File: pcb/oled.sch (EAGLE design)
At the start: 18 parts, among them U1 UG-2828GDEDF11, U3 FAN5331SX

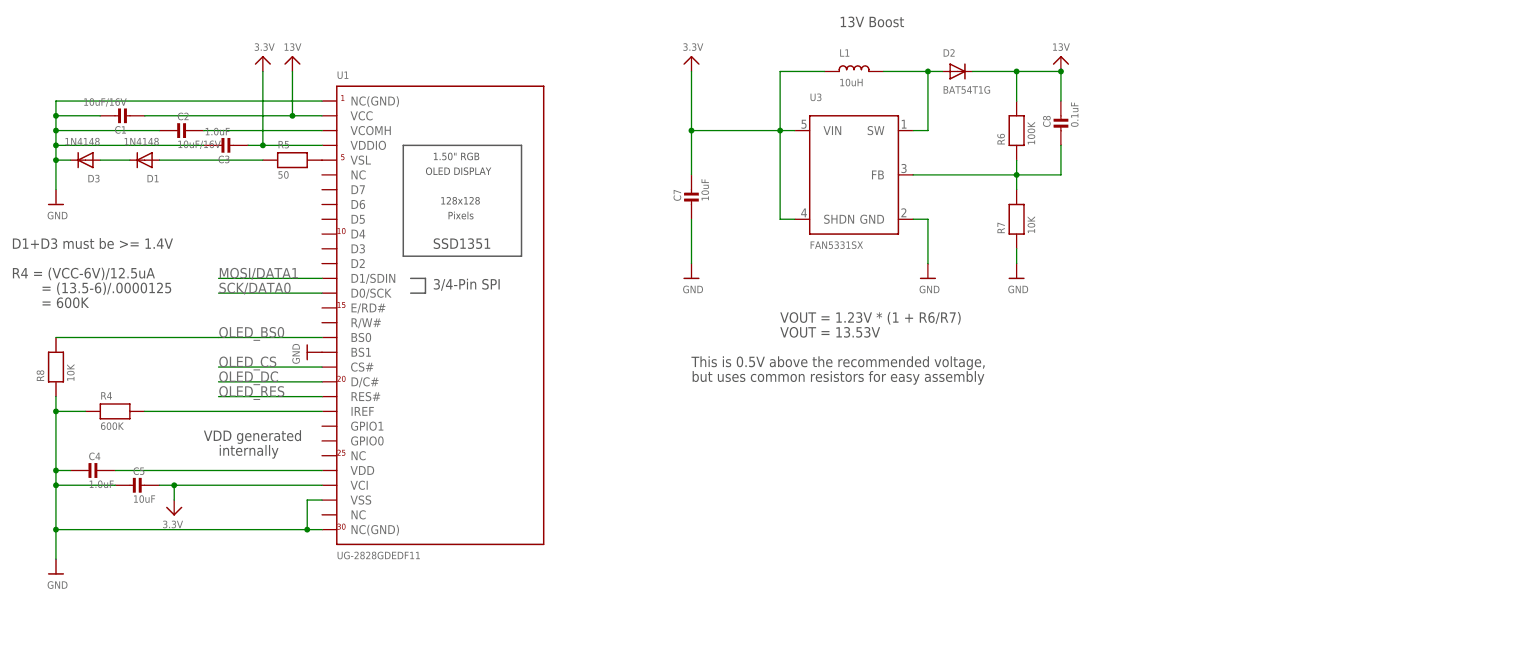
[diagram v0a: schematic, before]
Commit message: oled board ready to be fab'd
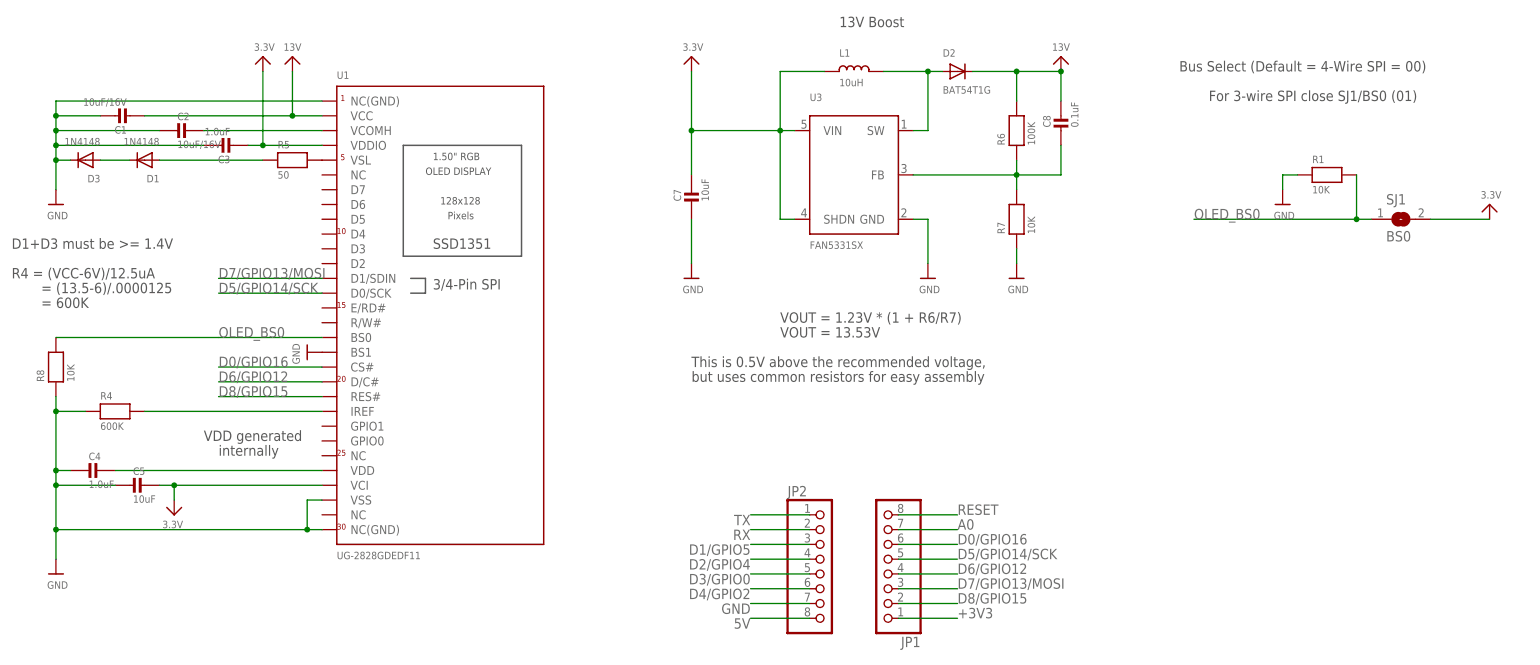
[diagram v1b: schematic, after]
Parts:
- added JP1, JP2: (no value), adafruit:PINHD-1X8CLEANBIG
- added R1: 10K, microbuilder:RESISTOR_0805MP
- added SJ1: BS0, microbuilder:SOLDERJUMPERREFLOW_NOPASTE
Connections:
- removed net 3.3V: C3.P$2, C5.P$1, C7.P$1, L1.1, U1.VCI, U1.VDDIO, U3.SHDN, U3.VIN
- removed net MOSI/DATA1: U1.D1/SDIN
- removed net OLED_CS: U1.CS#
- removed net OLED_DC: U1.D/C#
- removed net OLED_RES: U1.RES#
- removed net SCK/DATA0: U1.D0/SCK
- new net +3V3: C3.P$2, C5.P$1, C7.P$1, JP1.1, L1.1, SJ1.2, U1.VCI, U1.VDDIO, U3.SHDN, U3.VIN
- new net 5V: JP2.8
- new net A0: JP1.7
- new net D0/GPIO16: JP1.6, U1.CS#
- new net D1/GPIO5: JP2.3
- new net D2/GPIO4: JP2.4
- new net D3/GPIO0: JP2.5
- new net D4/GPIO2: JP2.6
- new net D5/GPIO14/SCK: JP1.5, U1.D0/SCK
- new net D6/GPIO12: JP1.4, U1.D/C#
- new net D7/GPIO13/MOSI: JP1.3, U1.D1/SDIN
- new net D8/GPIO15: JP1.2, U1.RES#
- new net RESET: JP1.8
- new net RX: JP2.2
- new net TX: JP2.1
- net GND: now also JP2.7, R1.1
- net OLED_BS0: now also R1.2, SJ1.1
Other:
- note added: "Bus Select (Default = 4-Wire SPI = 00)"
- note added: "For 3-wire SPI close SJ1/BS0 (01)"

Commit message: USB board schematic V2 done
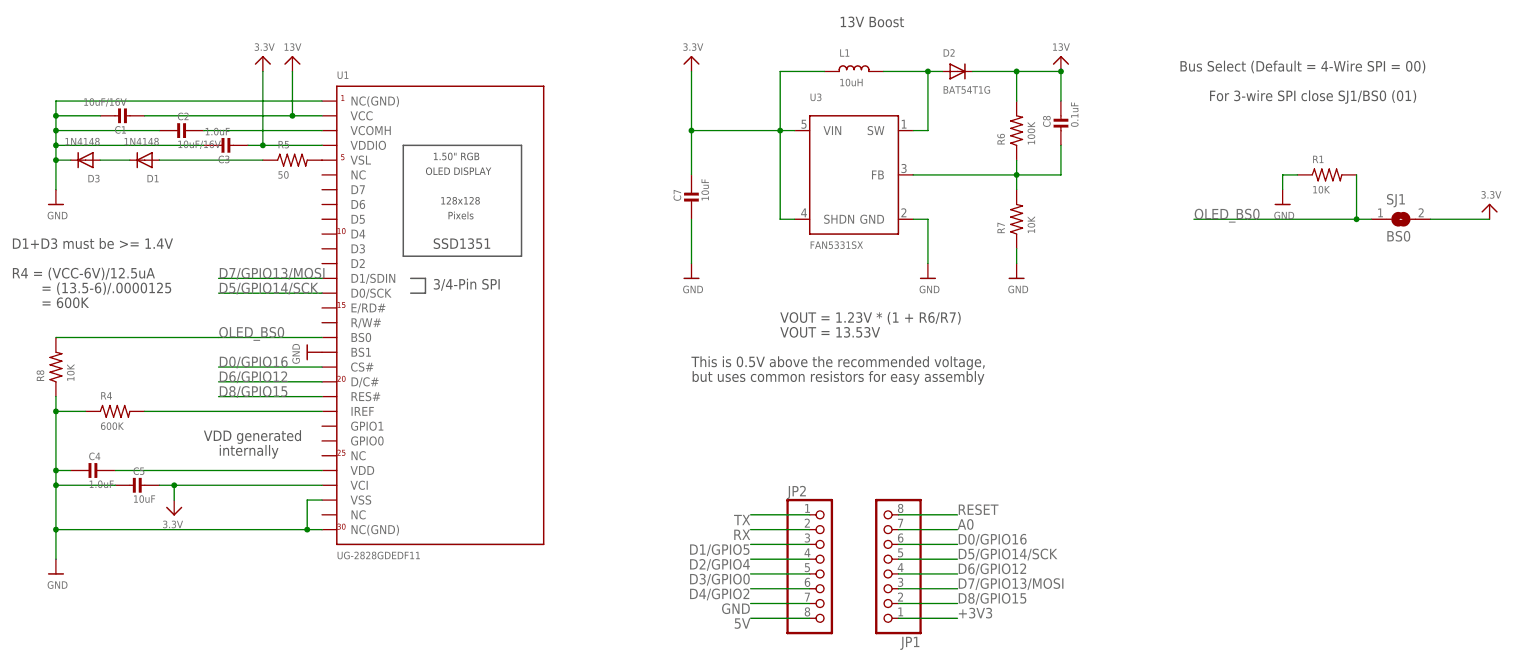
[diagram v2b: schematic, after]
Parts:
- R1: device microbuilder:RESISTOR_0805MP -> adafruit:R-US_R0805
- R4, R5, R6, R7, R8: device microbuilder:RESISTOR0805 -> adafruit:R-US_R0805
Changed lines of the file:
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@@
 <parts>
 <part name="U$4" library="microbuilder" deviceset="GND" device=""/>
-<part name="R4" library="microbuilder" deviceset="RESISTOR" device="0805" value="600K"/>
+<part name="R4" library="adafruit" library_urn="urn:adsk.eagle:library:420" deviceset="R-US_" device="R0805" package3d_urn="urn:adsk.eagle:package:6240566/1" value="600K"/>
 <part name="C1" library="microbuilder" deviceset="CAP_CERAMIC" device="0805" value="10uF/16V"/>
 <part name="C3" library="microbuilder" deviceset="CAP_CERAMIC" device="0805" value="1.0uF"/>
-<part name="R5" library="microbuilder" deviceset="RESISTOR" device="0805" value="50"/>
+<part name="R5" library="adafruit" library_urn="urn:adsk.eagle:library:420" deviceset="R-US_" device="R0805" package3d_urn="urn:adsk.eagle:package:6240566/1" value="50"/>
 <part name="D1" library="microbuilder" deviceset="DIODE" device="SOD-323" value="1N4148"/>
 <part name="C4" library="microbuilder" deviceset="CAP_CERAMIC" device="0805" value="1.0uF"/>
@@
 <part name="L1" library="microbuilder" deviceset="INDUCTOR" device="" value="10uH"/>
 <part name="D2" library="microbuilder" deviceset="DIODE" device="SOD-123" value="BAT54T1G"/>
-<part name="R6" library="microbuilder" deviceset="RESISTOR" device="0805" value="100K"/>
-<part name="R7" library="microbuilder" deviceset="RESISTOR" device="0805" value="10K"/>
+<part name="R6" library="adafruit" library_urn="urn:adsk.eagle:library:420" deviceset="R-US_" device="R0805" package3d_urn="urn:adsk.eagle:package:6240566/1" value="100K"/>
+<part name="R7" library="adafruit" library_urn="urn:adsk.eagle:library:420" deviceset="R-US_" device="R0805" package3d_urn="urn:adsk.eagle:package:6240566/1" value="10K"/>
 <part name="U$11" library="microbuilder" deviceset="GND" device=""/>
 <part name="U$12" library="microbuilder" deviceset="GND" device=""/>
@@
 <part name="D3" library="microbuilder" deviceset="DIODE" device="SOD-323" value="1N4148"/>
 <part name="U$3" library="microbuilder" deviceset="GND" device=""/>
-<part name="R8" library="microbuilder" deviceset="RESISTOR" device="0805" value="10K"/>
+<part name="R8" library="adafruit" library_urn="urn:adsk.eagle:library:420" deviceset="R-US_" device="R0805" package3d_urn="urn:adsk.eagle:package:6240566/1" value="10K"/>
 <part name="JP1" library="adafruit" library_urn="urn:adsk.eagle:library:420" deviceset="PINHD-1X8" device="CLEANBIG" package3d_urn="urn:adsk.eagle:package:6240708/1"/>
 <part name="JP2" library="adafruit" library_urn="urn:adsk.eagle:library:420" deviceset="PINHD-1X8" device="CLEANBIG" package3d_urn="urn:adsk.eagle:package:6240708/1"/>
 <part name="SJ1" library="microbuilder" deviceset="SOLDERJUMPER" device="REFLOW_NOPASTE" value="BS0"/>
-<part name="R1" library="microbuilder" deviceset="RESISTOR" device="_0805MP" value="10K"/>
+<part name="R1" library="adafruit" library_urn="urn:adsk.eagle:library:420" deviceset="R-US_" device="R0805" package3d_urn="urn:adsk.eagle:package:6240566/1" value="10K"/>
 <part name="U$2" library="microbuilder" deviceset="3.3V" device=""/>
 <part name="U$6" library="microbuilder" deviceset="GND" device=""/>

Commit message: Rework Oled board to use VIN
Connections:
- removed net 5V: JP2.8
- new net VIN: C7.P$1, JP2.8, L1.1, U3.SHDN, U3.VIN
- net +3V3: no longer C7.P$1, L1.1, U3.SHDN, U3.VIN

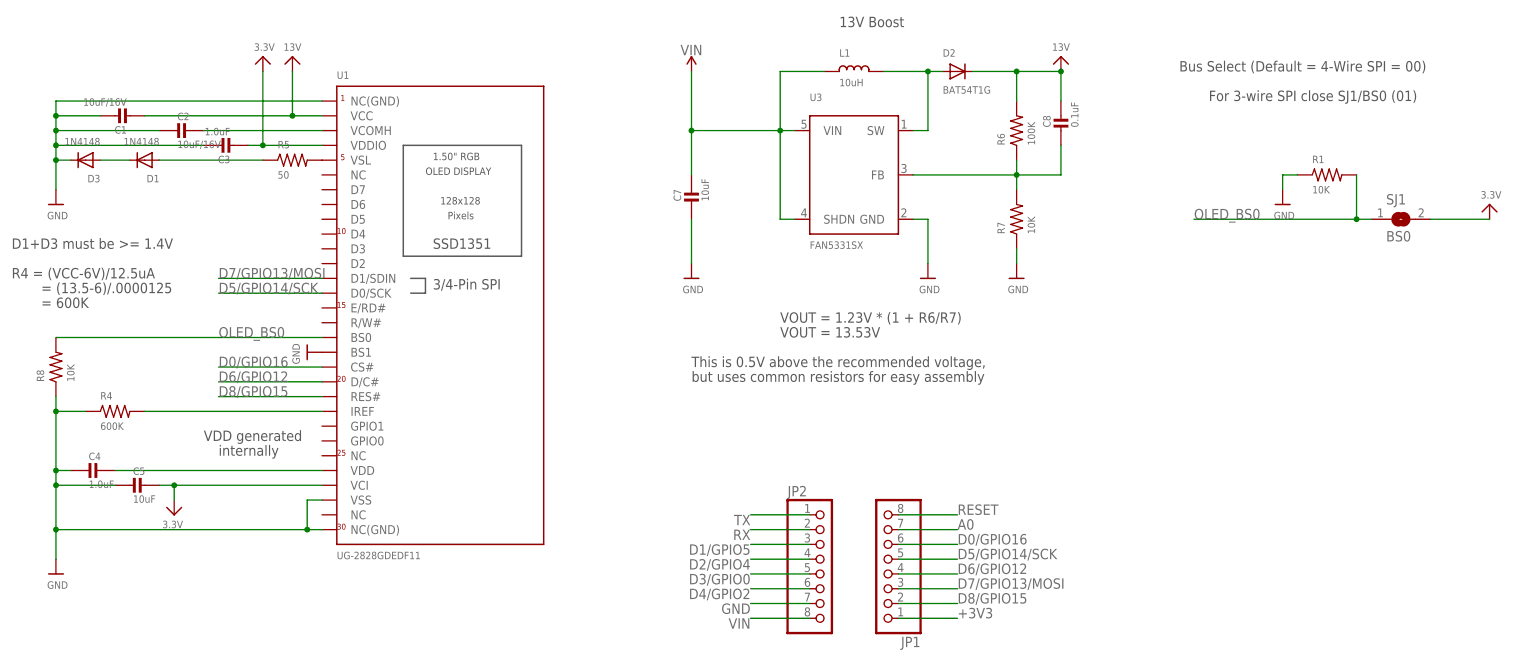
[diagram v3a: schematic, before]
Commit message: V2 oled board ordered
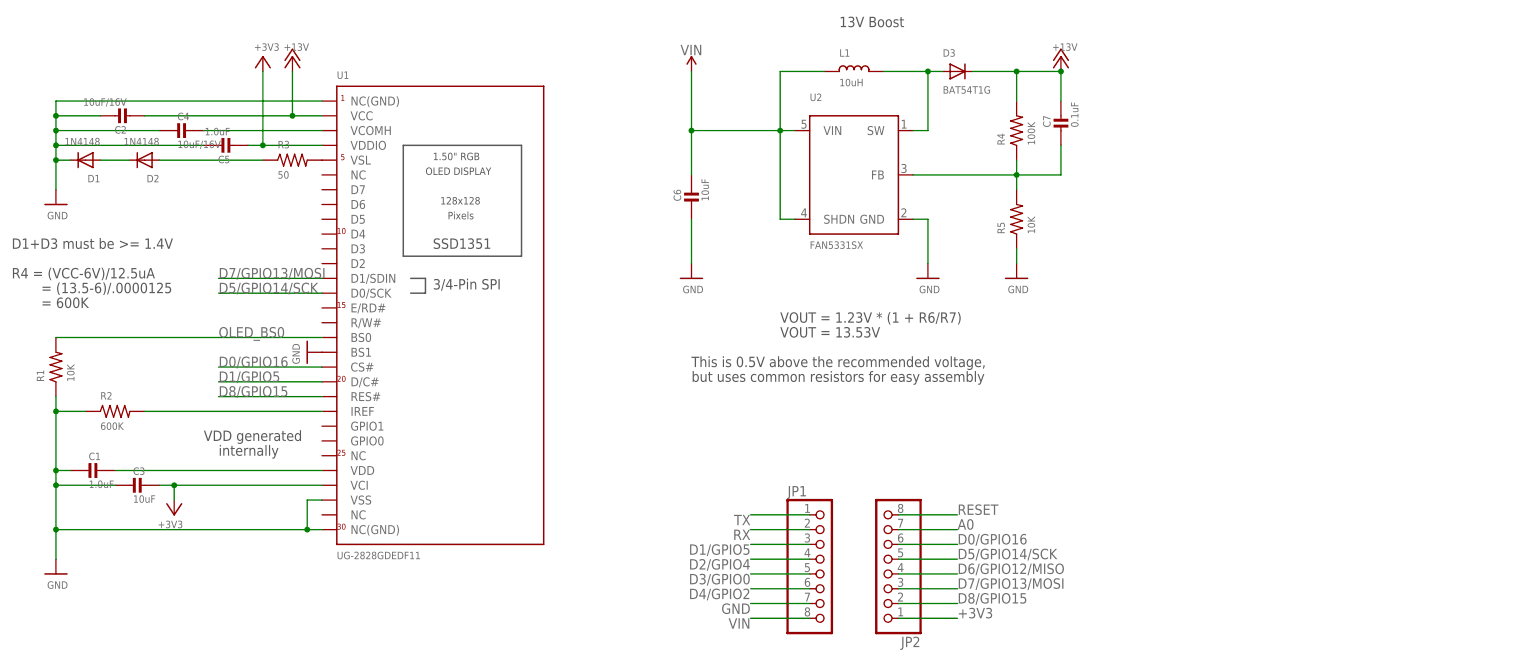
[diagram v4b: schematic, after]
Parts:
- removed C8: 0.1uF, microbuilder:CAP_CERAMIC0805
- removed R6: 100K, adafruit:R-US_R0805
- removed R7, R8: 10K, adafruit:R-US_R0805
- removed SJ1: BS0, microbuilder:SOLDERJUMPERREFLOW_NOPASTE
- added C6: 10uF, microbuilder:CAP_CERAMIC0805
- added R2: 600K, adafruit:R-US_R0805
- added R3: 50, adafruit:R-US_R0805
- C1: value 10uF/16V -> 1.0uF
- C3: value 1.0uF -> 10uF
- C4: value 1.0uF -> 10uF/16V
- C5: value 10uF -> 1.0uF
- C7: value 10uF -> 0.1uF
- D2: value BAT54T1G -> 1N4148; device microbuilder:DIODESOD-123 -> microbuilder:DIODESOD-323
- D3: value 1N4148 -> BAT54T1G; device microbuilder:DIODESOD-323 -> microbuilder:DIODESOD-123
- R4: value 600K -> 100K
- R5: value 50 -> 10K
- renumbered U3 to U2
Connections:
- removed net D6/GPIO12: JP1.4, U1.D/C#
- new net D6/GPIO12/MISO: JP2.4
- net +3V3: now also C3.P$1, C5.P$2, JP2.1; no longer C3.P$2, C5.P$1, JP1.1, SJ1.2
- net 13V: now also C2.P$2, C7.P$1, D3.C, R4.2; no longer C1.P$2, C8.P$1, D2.C, R6.2
- net A0: now also JP2.7; no longer JP1.7
- net D0/GPIO16: now also JP2.6; no longer JP1.6
- net D1/GPIO5: now also JP1.3, U1.D/C#; no longer JP2.3
- net D2/GPIO4: now also JP1.4; no longer JP2.4
- net D3/GPIO0: now also JP1.5; no longer JP2.5
- net D4/GPIO2: now also JP1.6; no longer JP2.6
- net D5/GPIO14/SCK: now also JP2.5; no longer JP1.5
- net D7/GPIO13/MOSI: now also JP2.3; no longer JP1.3
- net D8/GPIO15: now also JP2.2; no longer JP1.2
- net GND: now also C1.P$2, C2.P$1, C3.P$2, C5.P$1, C6.P$2, D1.C, JP1.7, R2.1, R5.1; no longer C1.P$1, C2.P$2, C3.P$1, C5.P$2, C7.P$2, D3.C, JP2.7, R4.1, R7.1, R8.1
- net IREF: now also R2.2; no longer R4.2
- net N$11: now also D1.A, D2.C; no longer D1.C, D3.A
- net N$3: now also C1.P$1; no longer C4.P$1
- net N$5: now also D3.A; no longer D2.A
- net N$6: now also R3.2; no longer R5.2
- net N$7: now also D2.A, R3.1; no longer D1.A, R5.1
- net N$8: now also C7.P$2, R4.1, R5.2; no longer C8.P$2, R6.1, R7.2
- net OLED_BS0: no longer R8.2, SJ1.1
- net RESET: now also JP2.8; no longer JP1.8
- net RX: now also JP1.2; no longer JP2.2
- net TX: now also JP1.1; no longer JP2.1
- net VCOMH: now also C4.P$1; no longer C2.P$1
- net VIN: now also C6.P$1, JP1.8; no longer C7.P$1, JP2.8
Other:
- note removed: "Bus Select (Default = 4-Wire SPI = 00)"
- note removed: "For 3-wire SPI close SJ1/BS0 (01)"
- moved on the sheet: C1, C2, C3, C4, C5, C7, D1, D2, D3, JP1, JP2, R1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

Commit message: Add a bunch of manufacturer part numbers to OLED board
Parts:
- C1, C5: MPN (none) -> C0805C105K4RAC7210
- C2, C3, C4, C6: MPN (none) -> EMK212ABJ106KG-T
- C7: MPN (none) -> 08051C104J4T4A
- D1, D2: MPN (none) -> 1N4148WS-E3-08
- D3: MPN (none) -> BAT54T1G
- JP1, JP2: POPULATE (none) -> 0
- L1: MPN (none) -> L0805R100MPWRT
- R1, R5: MPN (none) -> CRCW080510K0FKEAC
- R2: MPN (none) -> ERJ-6ENF5903V
- R3: MPN (none) -> CRCW080550R0FKTA
- R4: MPN (none) -> CR0805AFX-1003EAS
- U1: MPN (none) -> XF2M-3015-1A
- U2: MPN (none) -> FAN5331SX

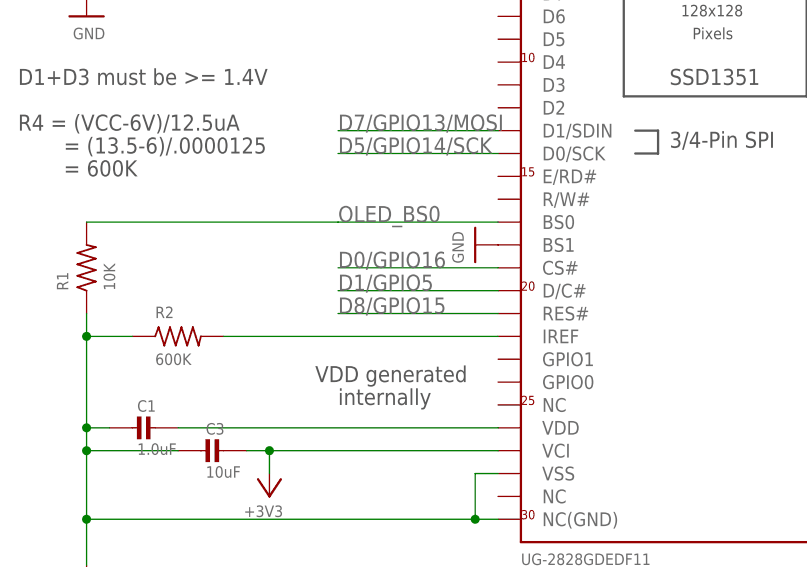
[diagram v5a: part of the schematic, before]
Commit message: Use GPIO2 instead of GPIO5(SCL) for OLED DC pin
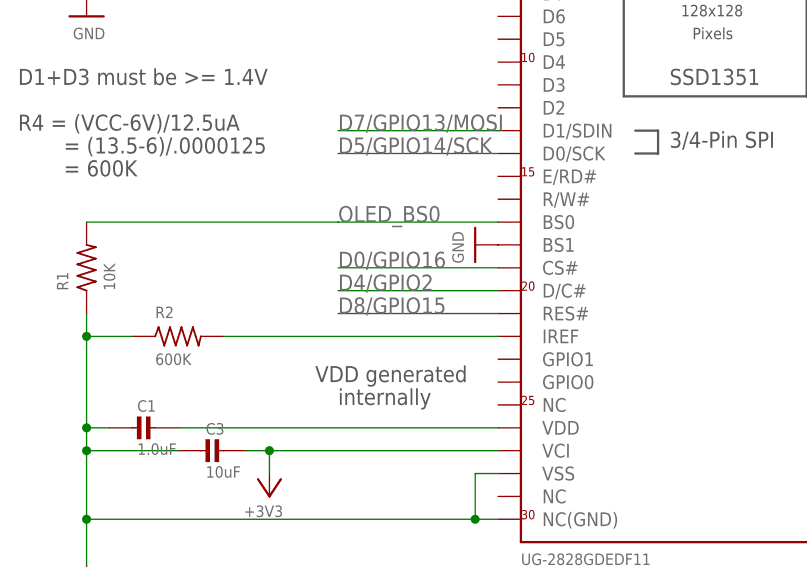
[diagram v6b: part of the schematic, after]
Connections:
- net D1/GPIO5: no longer U1.D/C#
- net D4/GPIO2: now also U1.D/C#
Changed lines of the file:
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@@
 <label x="203.2" y="96.52" size="1.778" layer="95" rot="R180"/>
-</segment>
-<segment>
-<wire x1="129.54" y1="124.46" x2="111.76" y2="124.46" width="0.1524" layer="91"/>
-<label x="111.76" y="124.46" size="1.778" layer="95"/>
-<pinref part="U1" gate="G$1" pin="D/C#"/>
 </segment>
 </net>
@@
 <label x="203.2" y="88.9" size="1.778" layer="95" rot="R180"/>
 </segment>
+<segment>
+<wire x1="129.54" y1="124.46" x2="111.76" y2="124.46" width="0.1524" layer="91"/>
+<label x="111.76" y="124.46" size="1.778" layer="95"/>
+<pinref part="U1" gate="G$1" pin="D/C#"/>
+</segment>
 </net>

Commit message: Oled board v3 ordered
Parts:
- JP1, JP2: MPN (none) -> 10129378-908001BLF
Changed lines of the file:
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@@
 </part>
 <part name="JP2" library="adafruit" library_urn="urn:adsk.eagle:library:420" deviceset="PINHD-1X8" device="CLEANBIG" package3d_urn="urn:adsk.eagle:package:6240708/1">
+<attribute name="MPN" value="10129378-908001BLF"/>
 <attribute name="POPULATE" value="0"/>
 </part>
 <part name="JP1" library="adafruit" library_urn="urn:adsk.eagle:library:420" deviceset="PINHD-1X8" device="CLEANBIG" package3d_urn="urn:adsk.eagle:package:6240708/1">
+<attribute name="MPN" value="10129378-908001BLF"/>
 <attribute name="POPULATE" value="0"/>
 </part>
@@
 <attribute name="VALUE" x="232.41" y="106.68" size="1.778" layer="96" rot="R180"/>
 <attribute name="POPULATE" x="226.06" y="91.44" size="1.778" layer="96" rot="R180" display="off"/>
+<attribute name="MPN" x="226.06" y="91.44" size="1.778" layer="96" rot="R180" display="off"/>
 </instance>
 <instance part="JP1" gate="G$1" x="215.9" y="93.98" smashed="yes">
@@
 <attribute name="VALUE" x="209.55" y="78.74" size="1.778" layer="96"/>
 <attribute name="POPULATE" x="215.9" y="93.98" size="1.778" layer="96" display="off"/>
+<attribute name="MPN" x="215.9" y="93.98" size="1.778" layer="96" display="off"/>
 </instance>
 <instance part="SUPPLY1" gate="G$1" x="193.04" y="177.8" smashed="yes">
